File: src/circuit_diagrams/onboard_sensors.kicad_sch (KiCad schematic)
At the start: 8 parts, among them U1 BMX055, U2 DPS310XTSA1, U7 ublox_SAM-M8Q

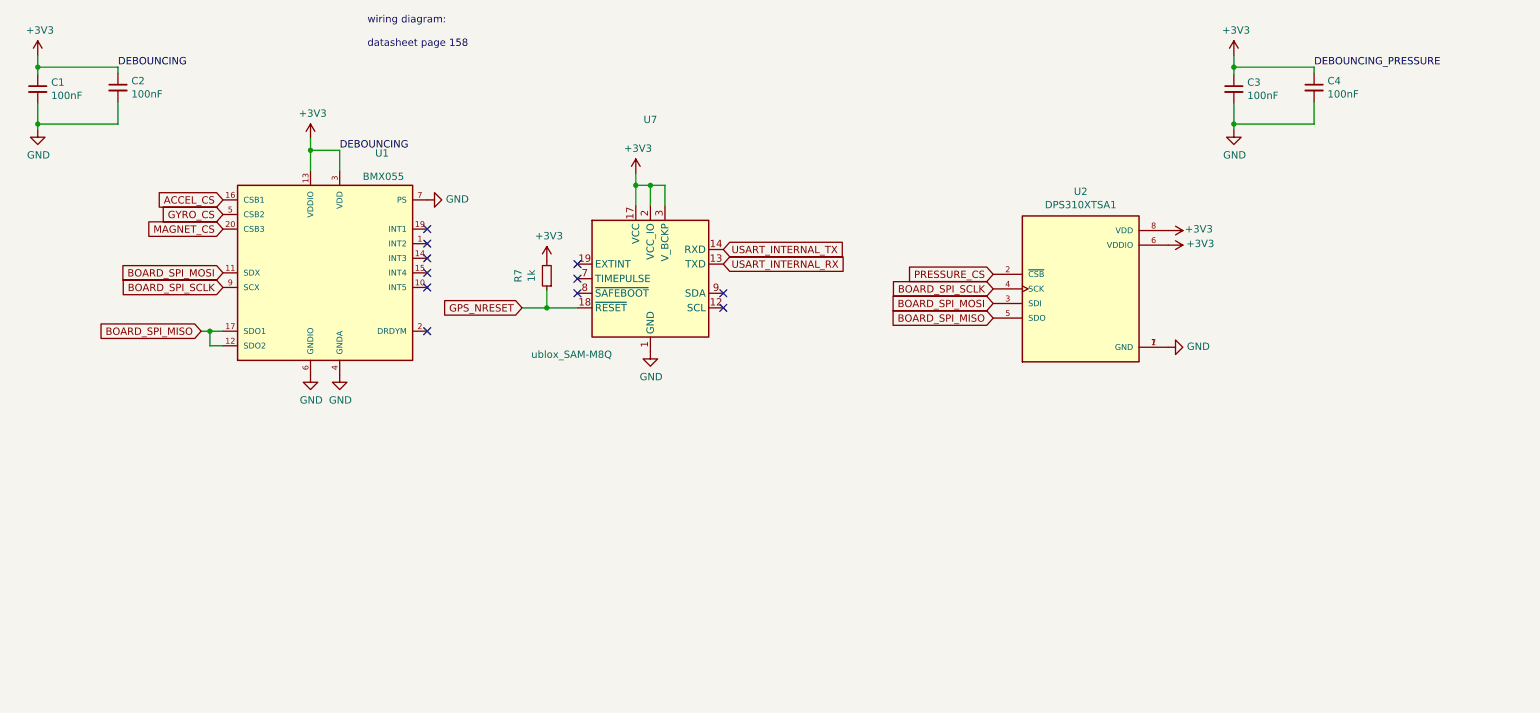
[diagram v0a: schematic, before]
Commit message: [DEVMINOR] Reorganization of the circuit diagram
Adding dividers and labels to subsections of the project
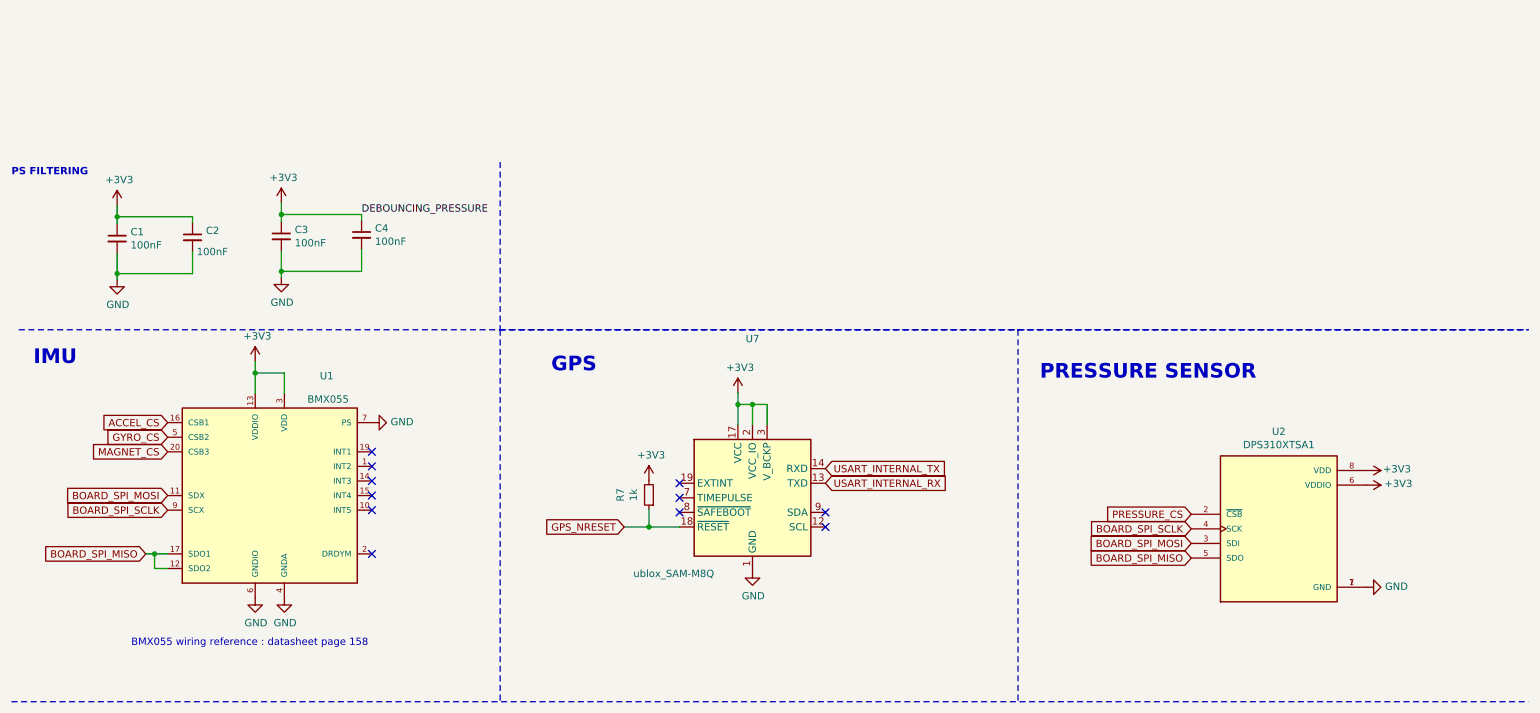
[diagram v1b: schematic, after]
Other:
- note added: "BMX055 wiring reference : datasheet page 158"
- note added: "GPS"
- note added: "IMU"
- note added: "PRESSURE SENSOR"
- note added: "PS FILTERING"
- note removed: "wiring diagram: datasheet page 158"
- moved on the sheet: C1, C2, C3, C4, R7, U1, U2, U7
